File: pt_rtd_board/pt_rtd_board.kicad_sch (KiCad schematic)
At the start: 33 parts, among them J1 DSUB 1, J2 DSUB 2, J3 DSUB 3, J4 PCIE Socket, U1 HX711_Breakout, U10 TCA9548A_Breakout, U2 HX711_Breakout, U3 HX711_Breakout, U4 HX711_Breakout, U5 HX711_Breakout, U6 HX711_Breakout, U7 HX711_Breakout, U8 HX711_Breakout, U9 HX711_Breakout

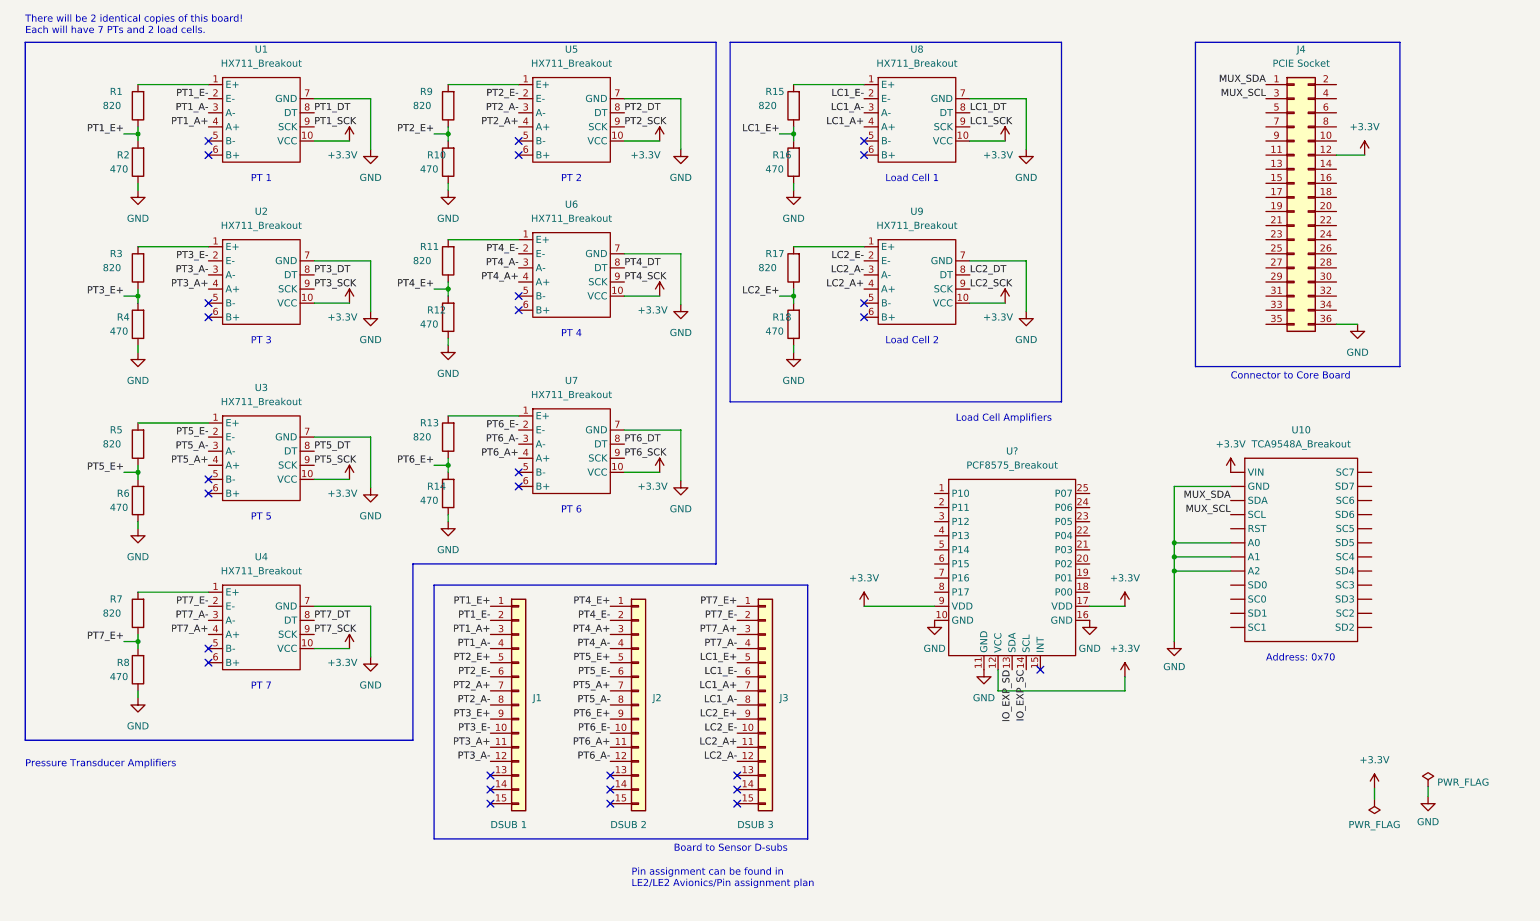
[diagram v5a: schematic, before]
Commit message: updating pin assignment + symbols
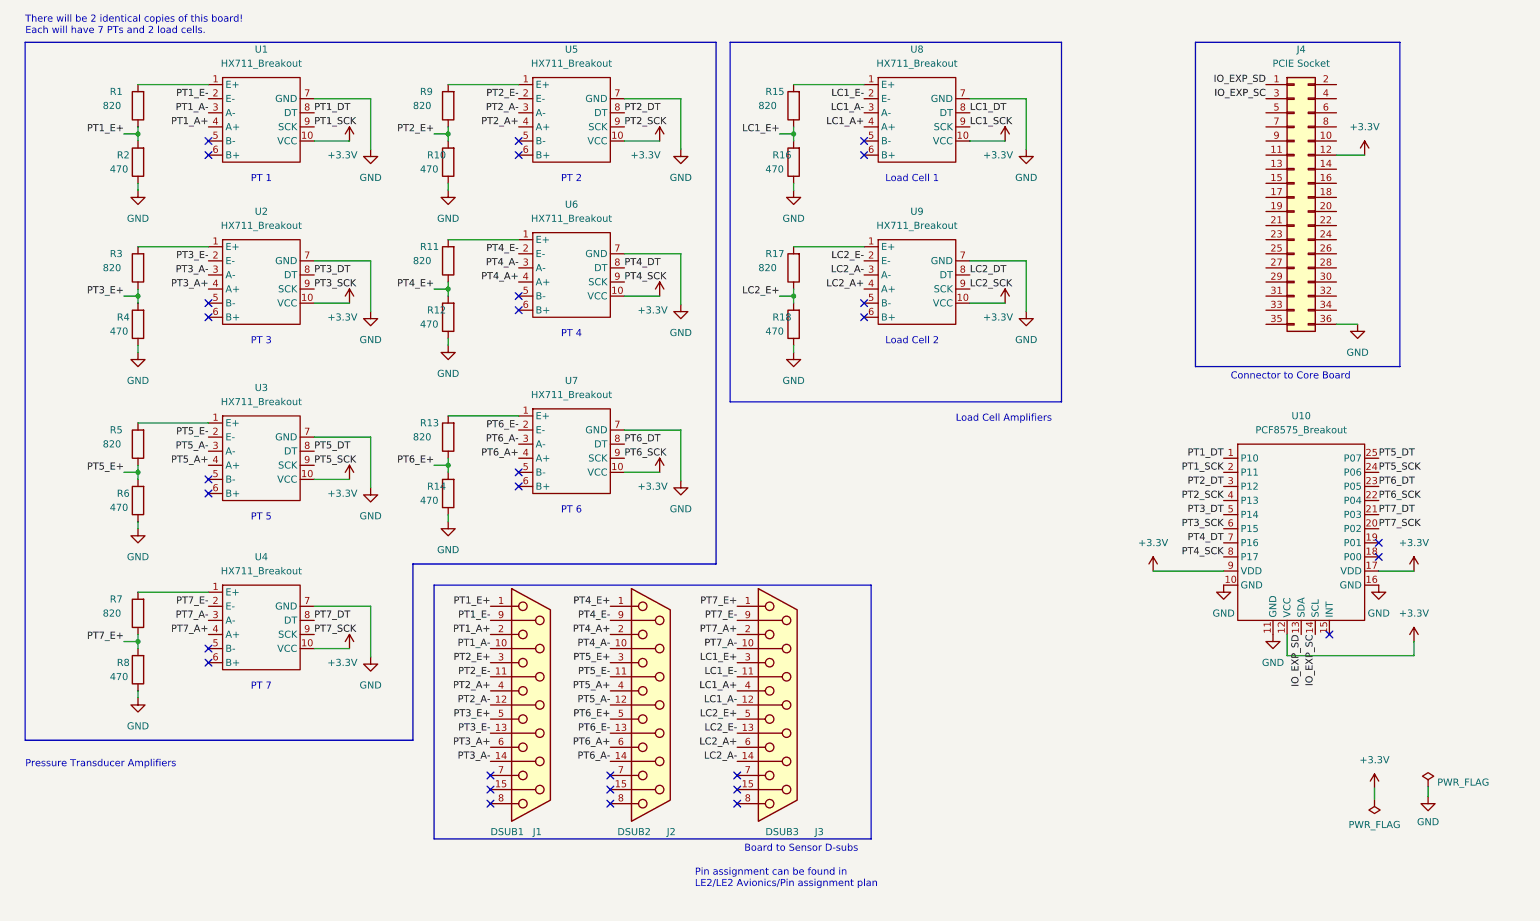
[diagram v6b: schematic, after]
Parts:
- removed J1: DSUB 1, symbol Connector_Generic:Conn_01x15
- removed J2: DSUB 2, symbol Connector_Generic:Conn_01x15
- removed J3: DSUB 3, symbol Connector_Generic:Conn_01x15
- removed U10: TCA9548A_Breakout, symbol TCA9548A_Breakout:TCA9548A_Breakout
- added J1: DSUB1, symbol Connector:DB15_Female
- added J2: DSUB2, symbol Connector:DB15_Female
- added J3: DSUB3, symbol Connector:DB15_Female
- gave numbers to parts that had none: 1
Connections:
- net MUX_SCL is gone; now on net IO_EXP_SC: J4.3 (Pin_3)
- net MUX_SDA is gone; now on net IO_EXP_SD: J4.1 (Pin_1)
- net LC1_A+: now also J3.4
- net LC1_A-: now also J3.12 (P12)
- net LC1_E+: now also J3.3
- net LC1_E-: now also J3.11 (P111)
- net LC2_A+: now also J3.6
- net LC2_A-: now also J3.14 (P14)
- net LC2_E+: now also J3.5
- net LC2_E-: now also J3.13 (P13)
- net PT1_A+: now also J1.2
- net PT1_A-: now also J1.10 (P10)
- net PT1_DT: now also U10.1 (P10)
- net PT1_E+: now also J1.1
- net PT1_E-: now also J1.9 (P9)
- net PT1_SCK: now also U10.2 (P11)
- net PT2_A+: now also J1.4
- net PT2_A-: now also J1.12 (P12)
- net PT2_DT: now also U10.3 (P12)
- net PT2_E+: now also J1.3
- net PT2_E-: now also J1.11 (P111)
- net PT2_SCK: now also U10.4 (P13)
- net PT3_A+: now also J1.6
- net PT3_A-: now also J1.14 (P14)
- net PT3_DT: now also U10.5 (P14)
- net PT3_E+: now also J1.5
- net PT3_E-: now also J1.13 (P13)
- net PT3_SCK: now also U10.6 (P15)
- net PT4_A+: now also J2.2
- net PT4_A-: now also J2.10 (P10)
- net PT4_DT: now also U10.7 (P16)
- net PT4_E+: now also J2.1
- net PT4_E-: now also J2.9 (P9)
- net PT4_SCK: now also U10.8 (P17)
- net PT5_A+: now also J2.4
- net PT5_A-: now also J2.12 (P12)
- net PT5_DT: now also U10.25 (P07)
- net PT5_E+: now also J2.3
- net PT5_E-: now also J2.11 (P111)
- net PT5_SCK: now also U10.24 (P06)
- net PT6_A+: now also J2.6
- net PT6_A-: now also J2.14 (P14)
- net PT6_DT: now also U10.23 (P05)
- net PT6_E+: now also J2.5
- net PT6_E-: now also J2.13 (P13)
- net PT6_SCK: now also U10.22 (P04)
- net PT7_A+: now also J3.2
- net PT7_A-: now also J3.10 (P10)
- net PT7_DT: now also U10.21 (P03)
- net PT7_E+: now also J3.1
- net PT7_E-: now also J3.9 (P9)
- net PT7_SCK: now also U10.20 (P02)
- no-connect marks 28 -> 30
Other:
- note removed: "Address: 0x70"
- moved on the sheet: U10

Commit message: updates to connector
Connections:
- net LC1_DT: now also U10.19 (P01)
- net LC1_SCK: now also U10.18 (P00)
- no-connect marks 30 -> 28
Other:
- note added: "Broadcast pin?"
- note added: "GPIO Expander"
- note added: "Where to connect 2nd LC"
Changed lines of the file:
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@@
   (no_connect (at 49.53 68.58))
   (no_connect (at 49.53 100.33))
-  (no_connect (at 260.35 111.76))
   (no_connect (at 49.53 36.83))
   (no_connect (at 105.41 67.31))
@@
   (no_connect (at 167.64 68.58))
   (no_connect (at 49.53 39.37))
-  (no_connect (at 260.35 109.22))
   (no_connect (at 49.53 130.81))
   (no_connect (at 167.64 39.37))
@@
     (stroke (width 0) (type default) (color 0 0 0 0))
   )
+  (polyline (pts (xy 215.9 83.82) (xy 217.17 83.82))
+    (stroke (width 0) (type default) (color 0 0 0 0))
+  )
   (wire (pts (xy 266.7 129.54) (xy 266.7 127))
     (stroke (width 0) (type default) (color 0 0 0 0))
@@
     (stroke (width 0) (type default) (color 0 0 0 0))
   )
+  (polyline (pts (xy 215.9 83.82) (xy 276.86 83.82))
+    (stroke (width 0) (type default) (color 0 0 0 0))
+  )
   (wire (pts (xy 186.69 66.04) (xy 193.04 66.04))
     (stroke (width 0) (type default) (color 0 0 0 0))
@@
     (stroke (width 0) (type default) (color 0 0 0 0))
   )
+  (polyline (pts (xy 276.86 139.7) (xy 215.9 139.7))
+    (stroke (width 0) (type default) (color 0 0 0 0))
+  )
   (wire (pts (xy 92.71 95.25) (xy 92.71 96.52))
     (stroke (width 0) (type default) (color 0 0 0 0))
@@
     (stroke (width 0) (type default) (color 0 0 0 0))
   )
+  (polyline (pts (xy 276.86 83.82) (xy 276.86 139.7))
+    (stroke (width 0) (type default) (color 0 0 0 0))
+  )
   (wire (pts (xy 92.71 104.14) (xy 92.71 105.41))
     (stroke (width 0) (type default) (color 0 0 0 0))
@@
     (stroke (width 0) (type default) (color 0 0 0 0))
   )
+  (polyline (pts (xy 215.9 139.7) (xy 215.9 83.82))
+    (stroke (width 0) (type default) (color 0 0 0 0))
+  )
   (wire (pts (xy 68.58 128.27) (xy 74.93 128.27))
     (stroke (width 0) (type default) (color 0 0 0 0))
@@
     (stroke (width 0) (type default) (color 0 0 0 0))
   )
-  (wire (pts (xy 260.35 114.3) (xy 266.7 114.3))
+  (wire (pts (xy 260.35 114.3) (xy 273.05 114.3))
     (stroke (width 0) (type default) (color 0 0 0 0))
   )
@@
     (effects (font (size 1.27 1.27)) (justify left bottom))
   )
+  (text "Broadcast pin?" (at 210.82 55.88 0)
+    (effects (font (size 1.27 1.27)) (justify left bottom))
+  )
   (text "PT 7\n" (at 57.15 135.89 0)
     (effects (font (size 1.27 1.27)) (justify left bottom))
@@
   )
   (text "PT 5\n" (at 57.15 105.41 0)
+    (effects (font (size 1.27 1.27)) (justify left bottom))
+  )
+  (text "Where to connect 2nd LC" (at 172.72 78.74 0)
     (effects (font (size 1.27 1.27)) (justify left bottom))
   )
@@
     (effects (font (size 1.27 1.27)) (justify left bottom))
   )
+  (text "GPIO Expander" (at 256.54 142.24 0)
+    (effects (font (size 1.27 1.27)) (justify left bottom))
+  )
   (label "PT6_A-" (at 121.92 148.59 180)
     (effects (font (size 1.27 1.27)) (justify right bottom))
@@
     (effects (font (size 1.27 1.27)) (justify left bottom))
   )
+  (label "LC1_DT" (at 260.35 109.22 0)
+    (effects (font (size 1.27 1.27)) (justify left bottom))
+  )
   (label "LC2_A+" (at 144.78 146.05 180)
     (effects (font (size 1.27 1.27)) (justify right bottom))
@@
   (label "LC2_E+" (at 152.4 64.77 180)
     (effects (font (size 1.27 1.27)) (justify right bottom))
+  )
+  (label "LC1_SCK" (at 260.35 111.76 0)
+    (effects (font (size 1.27 1.27)) (justify left bottom))
   )
   (label "LC1_A-" (at 167.64 31.75 180)
@@
     (pin "1")
   )
-  (symbol (lib_id "power:+3.3V") (at 266.7 114.3 0) (unit 1)
-    (in_bom yes) (on_board yes) (fields_autoplaced)
-    (property "Reference" "#PWR0106" (id 0) (at 266.7 118.11 0)
-      (effects (font (size 1.27 1.27)) hide)
-    )
-    (property "Value" "+3.3V" (id 1) (at 266.7 109.22 0))
-    (property "Footprint" "" (id 2) (at 266.7 114.3 0)
-      (effects (font (size 1.27 1.27)) hide)
-    )
-    (property "Datasheet" "" (id 3) (at 266.7 114.3 0)
-      (effects (font (size 1.27 1.27)) hide)
-    )
+  (symbol (lib_id "power:+3.3V") (at 273.05 114.3 0) (unit 1)
+    (in_bom yes) (on_board yes) (fields_autoplaced)
+    (property "Reference" "#PWR0106" (id 0) (at 273.05 118.11 0)
+      (effects (font (size 1.27 1.27)) hide)
+    )
+    (property "Value" "+3.3V" (id 1) (at 273.05 109.22 0))
+    (property "Footprint" "" (id 2) (at 273.05 114.3 0)
+      (effects (font (size 1.27 1.27)) hide)
+    )
+    (property "Datasheet" "" (id 3) (at 273.05 114.3 0)
+      (effects (font (size 1.27 1.27)) hide)
+    )
